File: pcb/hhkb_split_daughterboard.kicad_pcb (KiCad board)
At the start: 2 copper layers, 21 x 32 mm, 11 parts

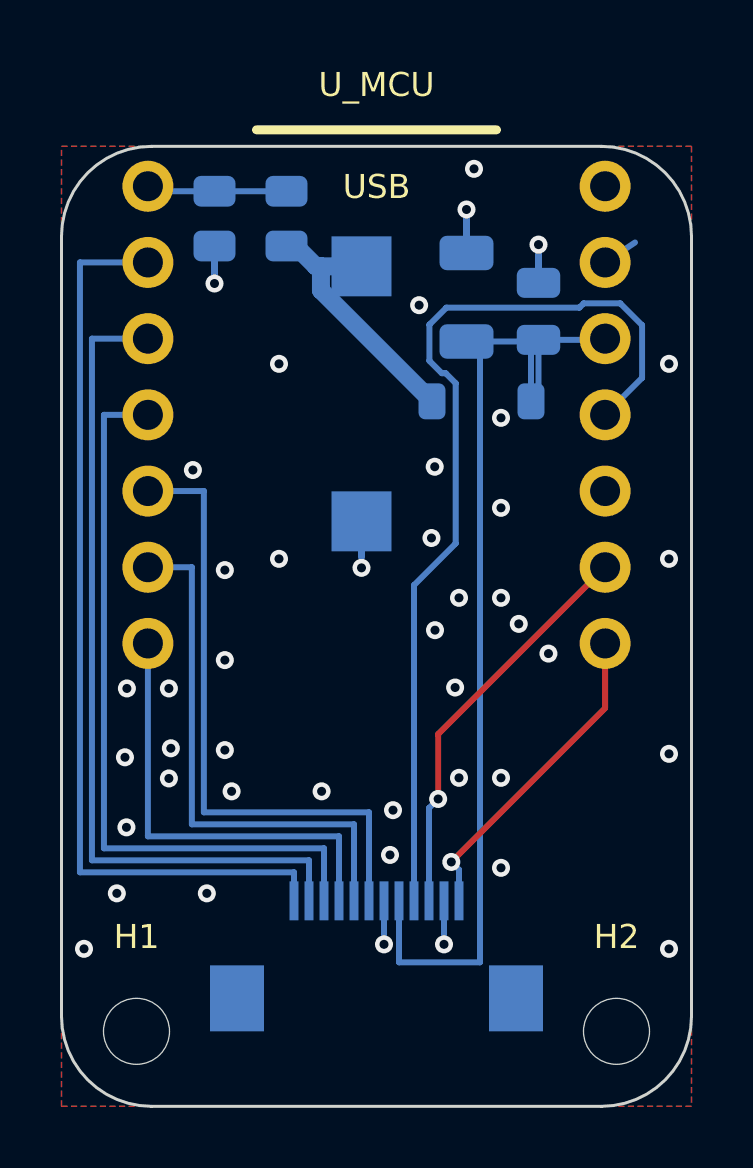
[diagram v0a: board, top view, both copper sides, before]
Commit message: 子基板の手配線の直角を、最小の 45 度 2 回に割った
利用者の指示「可能な限り最小のコーナーで 135 度 *2 に」。直角のまま
曲げると外側の角で銅が尖り、エッチングで過剰腐食を受けやすい。

点列を引く 3 か所（外側レーン・内側レーン・V3V3）が同じ形をしていたので、
面取り付きの `_polyline` に集約した。今後経路を変えても面取りは残る。

一辺は線幅と同じ 0.2mm。**見た目はほぼ角のまま**で、外側の角だけが
消えて 135 度が 2 つになる。それ以上大きくしても角の鋭さは変わらない。
線分が短くて両側に取れない折れは、その半分までに切り詰める。

実測: 45 度の区間が 20 本（配線後の基板でも 34 本残っている）。
子基板 DRC は 未配線 0 / 違反 1 で、面取りによる新しい違反は無い
（残る 1 件は V3V3 と GND ビアの 0.100mm。利用者の指示で保留中）。

Co-Authored-By: Claude Opus 5 (1M context) <noreply@anthropic.com>
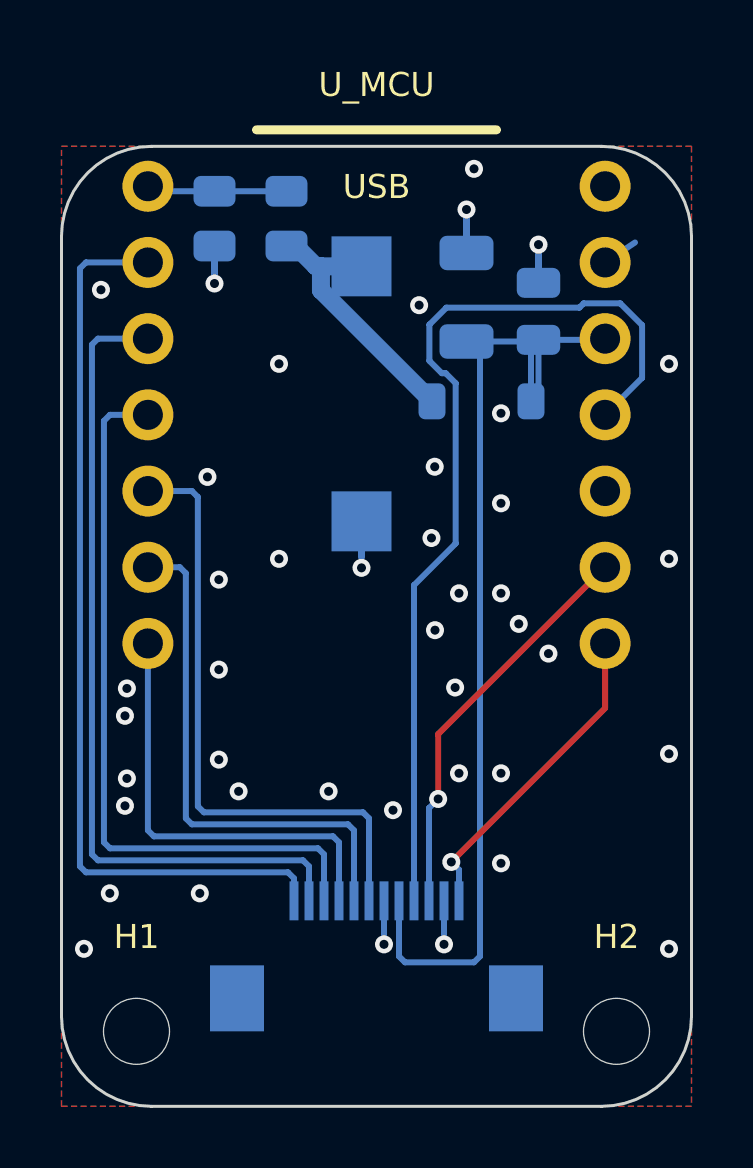
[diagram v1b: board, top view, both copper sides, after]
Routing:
- net GND: vias 44 -> 42

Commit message: 子基板の右列を、左列の鏡像として自分で引いた
利用者の指示「D1〜D6 を完璧に真似る形で、左右対称に」。右列は
Freerouting 任せだったので、左列と同じ規則で引くようにした。

XIAO は x=150.0 を挟んで左右対称なので、**鏡像は同じ y のパッドどうし**
（D1↔GND / D2↔3V3 / D3↔D10 / D4↔D9 / D5↔D8 / D6↔D7）。FFC は
n ↔ 13-n で写る。`_prewire_rows` に `side`（-1 左 / +1 右）を入れ、
左向きの直書き（min・-DB_W/2）を符号 1 つに畳んだ。

指摘を 3 つ受けて直した:
  - D7 が垂直に伸びていない … D6 の鏡像は D7。GND を外したことと
    垂直の有無は無関係だった
  - D4 の鏡像は D9 … 内側の順序を左列の鏡像 (D7,D8,D9) に揃えた
  - V3V3 が 2 経路で FFC に繋がる … `_prewire_power` の旧経路を削除。
    3V3 パッド ↔ FFC 2 番はレーンが引くので二重だった

**GND はレーンに載せず地板で受ける**（利用者の判断）。そのぶん外側は
2 本になるが、**位置は 3 本ぶんの幅に散らして真ん中を空ける**——
利用者の指示「D10 と離す意図で、鏡像の 3 本ラインの左端と右端と同様に」。
電源とデータ線の並走結合を、空いている枠を使って 0 コストで下げる。

⚠️ **この組み替えでケーブルの GND が 2 本から 1 本になった。**
SCK から最寄りの GND までが 0.5mm → 2.0mm に伸びている。効くのは
遷移が速い SCK 1 本で、どれだけ悪化するかは実測していない。
逃げ道は決めてある（D9=SPARE2 を両基板で GND へジャンパ）。

検査は「GND が 2 本」を数えるのをやめ、**距離そのもの**を見るように
書き換えた（`test_how_far_the_return_path_is`）。本数は手段で、目的は
戻り経路の短さ。故意に壊して距離 7 で落ちることを確認した。
`test_the_rules_actually_bite` の変異 1 件が**元と同じ値を代入する
空振り**になっていたのも、その検査自身が捕まえたので直した。

子基板 DRC: 違反 0 / 未配線 0。保留していた V3V3-GND の 0.100mm も
旧経路の削除で消えた。主基板の SPARE/SPARE2 が片側 1 ピンなので
test_circuit が 2 件赤。左右の基板はこれから直す。

Co-Authored-By: Claude Opus 5 (1M context) <noreply@anthropic.com>
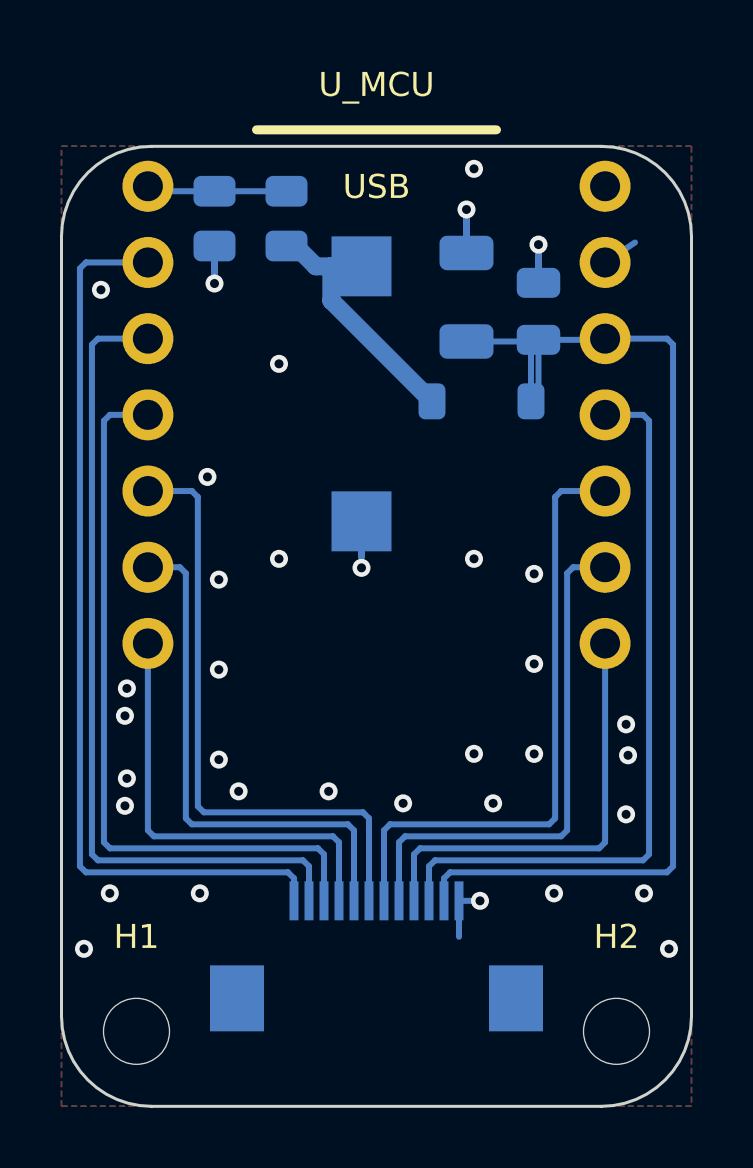
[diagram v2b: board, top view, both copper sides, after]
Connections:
- J_MAIN pad 1: CS -> GND
- J_MAIN pad 2: GND -> V3V3
- J_MAIN pad 3: SPI_SCK -> SPI_MOSI
- J_MAIN pad 4: SPI_MOSI -> CS
- J_MAIN pad 5: V3V3 -> SPI_SCK
- J_MAIN pad 6: GND -> SPARE2
- U_MCU pad D9: (no net) -> SPARE2
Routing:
- net SPARE2: track 0.00 -> 20.7 mm
- net SPI_MOSI: track 31.4 -> 24.6 mm
- net SPI_SCK: track 13.6 -> 17.6 mm, vias 1 -> 0
- net CS: track 10.8 -> 14.7 mm, vias 1 -> 0
- net GND: track 16.8 -> 13.4 mm, vias 42 -> 35
- net V3V3: track 34.2 -> 37.0 mm

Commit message: 行のネット名を「ケーブル上の位置」にし、行の並びを左右で別々に決めた
利用者の指摘「左右で ROW の順番を変えてもいい（左右で違う FW になるのは
確定している）。そういう意味で、DB の ROWx というピン名前付は不適切に
なるかもしれません」。理由は「左右 MAIN PCB を可能な限り鏡像にしている
がゆえに、どの FFC ピンがどの行に最適かが変わってくる」。

**ネット名を ROW0..4 → ROW_A..E に改めた。**名前が指すのは行番号ではなく
**ケーブル上の位置**（子基板のレーン）。行番号を名前にすると、左右で違う
行を同じ線に載せた瞬間に嘘になる（左の ROW2 が右では行 4 を運ぶ）。

**`row-gpios` を共通の dtsi から左右の overlay へ移した。**行がどの GPIO に
来るかは左右で物理的に違う——J_DB が左は板の右端・右は左端にあり、同じ
FFC のピンでも行バスへ近づく向きが逆。共通に 1 つだけ書くと、どちらかの
基板で必ず交差が出る。`matrix.row_nets(half)` が唯一の出所になった。

**割り当ての考え方も利用者の指摘で組み直した。**当初は「上へ行く群／下へ
行く群」で交差を数えていたが、正しくは **J_DB から遠い行ほど、パッド列で
「板の内側」の枠へ**。遠くまで行く枝を内側に置くと他の枝を跨がずに列を
離れられる。左右で並びが逆になる（12 番の板端／内側の意味が入れ替わる）。

    左: 行4=ROW_E 行3=ROW_D 行0=ROW_C 行2=ROW_B 行1=ROW_A
    右: 行4=ROW_A 行3=ROW_B 行0=ROW_C 行2=ROW_D 行1=ROW_E

**3 基板とも DRC 違反 0 / 未配線 0。**逆向きだと左 1 本・右 3 本が未配線に
なることを実測した（総当たりのモデルだけでは決まらなかった）。

検査は新しい構造に合わせて書き換え、**故意に壊して落ちることを確認した**
（overlay のピンを 1 つ変える／行を 2 つ入れ替える）。「左右で並びが違って
よい」ことも検査に書いて、揃える方向の変更が入らないようにした。

⚠️ 主基板の SPARE/SPARE2 が片側 1 ピンなので test_circuit が 2 件赤。
これは左右基板の残作業（J_DB の予備ピンの行き先）で解消する。

Co-Authored-By: Claude Opus 5 (1M context) <noreply@anthropic.com>
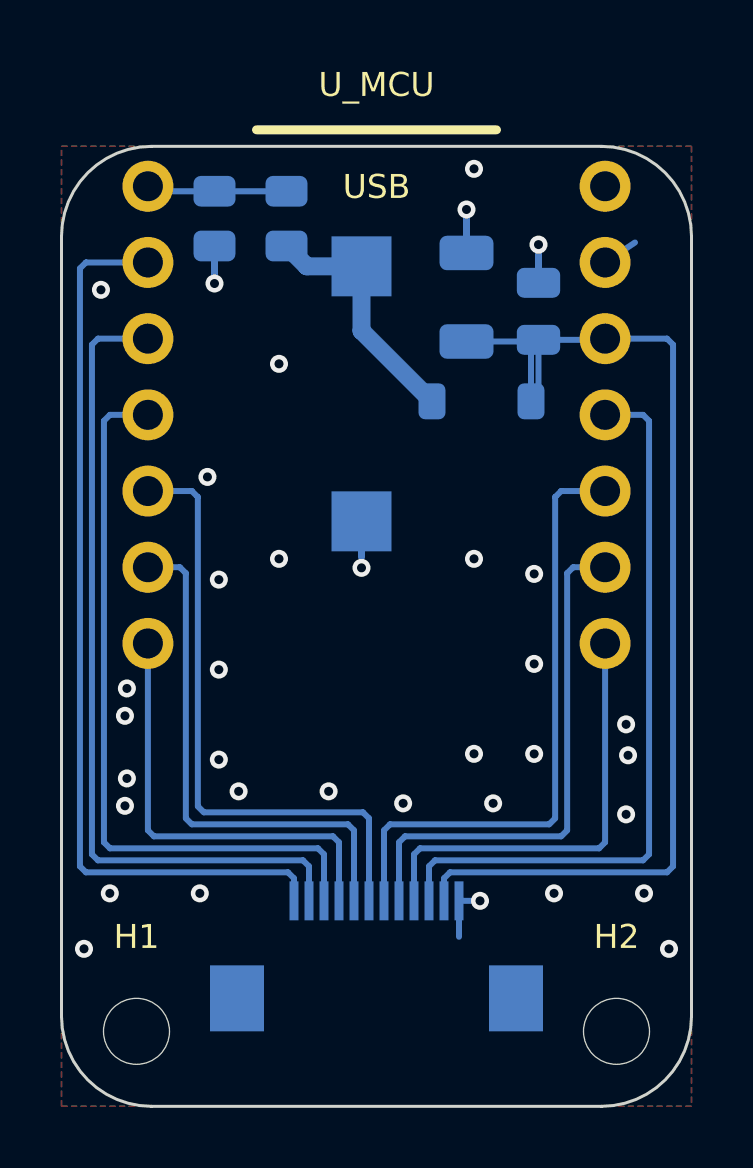
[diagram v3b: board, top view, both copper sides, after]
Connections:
- net ROW0 renamed ROW_E
- net ROW1 renamed ROW_C
- net ROW2 renamed ROW_D
- net ROW3 renamed ROW_A
- net ROW4 renamed ROW_B

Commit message: 子基板の未配線 4 件を消し、GND スタブの重複とシルクを直した
**未配線 4 件（VBATT_SW / VBATT_SENSE）の正体は Freerouting への入力だった。**
DSN に `(autoroute_settings)` があるだけで、Freerouting 2.3.0 が子基板の
ネットを 1 本も見なくなる。同じ DSN でブロックの有無だけを変えた実測:

    あり … "started with 0 unrouted nets" / SES 18 行（空）
    なし … "started with 4 unrouted nets" / SES 98 行

中身は関係ない（fanout / start_ripup_costs / layer_rule を 4 通り試して
すべて 0）。4 接続は直線経路に障害物が無く（2.2〜4.0mm・邪魔なし）、
「密集して引けない」のではなく**渡っていなかった**。子基板だけ外す。
主基板は正常に働く（左 started_with=60）ので残す。

**GND の引き出しが 1 パッドに 2 本生えていた**（利用者「GND は同じベタに
2 つ生えています。両方いるか、という事です」）。`_prewire_power` と
`gnd_fanout.place` がどちらも同じパッドから B.Cu へ出るため、6 パッドに
11 本。うち 4 組は始点も向きも同じで、1.2mm 側はビアへ向かうスタブの
完全な部分区間だった。ビアで受けるパッドには引かない。

さらに **U_MCU の GND は PTH**（穴 1.0mm）で、穴自体が両面のベタを貫く
ので引き出しは元から不要だった。「最寄りビアまで 3.22mm」と書いたのは
スタブの端から測った誤りで、中心からは 2.13mm。そもそも距離の問題では
なかった。引き出しは 11 本 → 0 本になり、未配線は増えていない。

**肩の高さを左右で揃えた**（利用者「この微妙に高さ違うのを直してほしい」）。
`over` を `i`（この列の何本目か）ではなく `slot`（枠の番号）で数える。
本数の違う列で同じ役割の線が違う高さになっていた。交差は増えない
（全 11 ネットを総当たりで交差判定して 0 件）。V3V3 だけは鏡像にならないが
利用者の判断で現状維持。

**V3V3 の往復を消した**（利用者「C_DB と D_PWR の間で不要に 2 本」）。
x 順の鎖に、一列から 2mm 下がった D_PWR が挟まって往復していた。
横一列のものだけで鎖を作り、外れたものは最寄りへ 1 本。

**ビアの空白を埋めた**（利用者「D6, D7 の下の領域、GND とビア打てないの？」）。
格子は λ/10 = 6.5mm と粗く、21x32mm では格子点が十数個しかないので
1 点が塞がると周りが丸ごと空く。実測で打てる点が 168 箇所あったのに
0 個だった。ピッチは動かさず、外れた点だけ半ピッチ以内で探し直す。
格子 7 → 14 個。

**シルクは利用者が KiCad で並べたものを出所にする**（`POWER_PLACE` と同じ）。
4 方向を試して空きを探す実装を書いたが、判定を厳しくするほど
「どこも当たる＝動かさない」が増え、13 → 10 → 13 → 15 件と悪化した。
機械的な 4 方向では解が無い。`SILK_REF` に固定し、並べ直したときは
`_read_silk_from` で吸い出す（手で書き写さない）。

R_HI / SW_PWR の配置も利用者の基板から読み直した（11 部品すべて一致）。

子基板: 違反 0 / 未配線 0 / 警告 13 → 5。基板の検査 90 件通過。

Co-Authored-By: Claude Opus 5 (1M context) <noreply@anthropic.com>
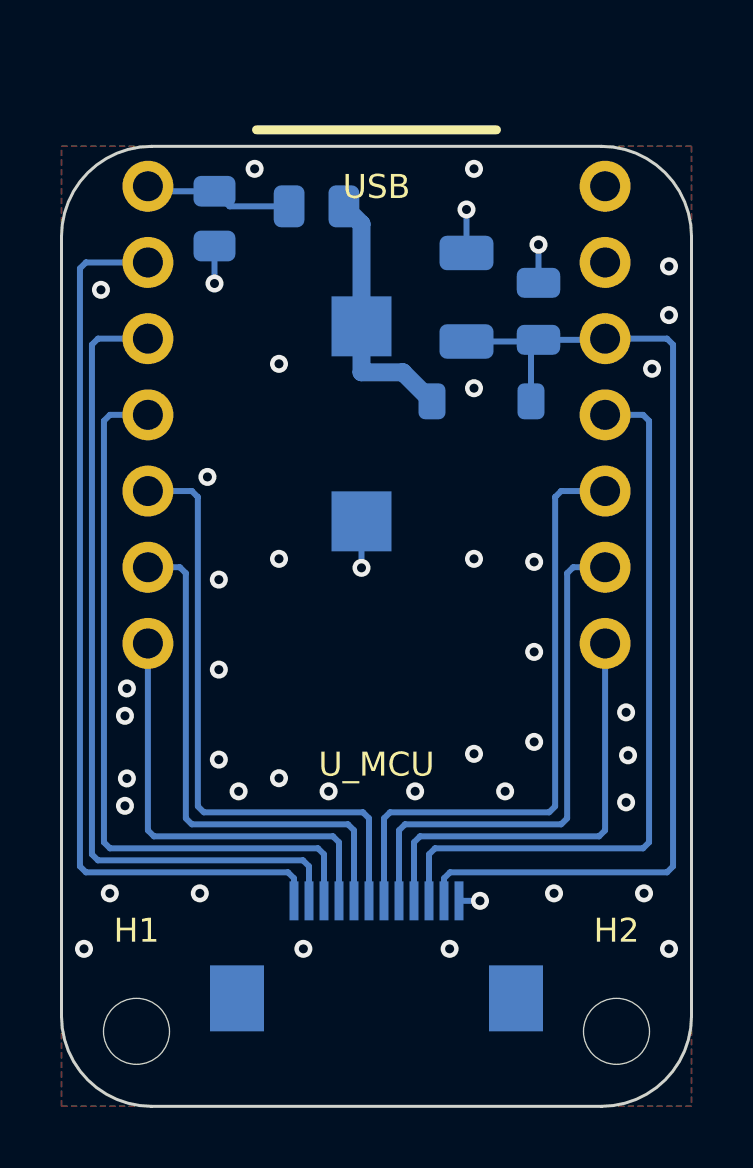
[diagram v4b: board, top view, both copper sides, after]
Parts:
- moved SW_PWR_1 2.00 mm to (149.5, 90.0)
- moved R_HI 1.08 mm to (148.0, 86.0), turned to 180 degrees
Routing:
- net GND: track 13.4 -> 6.23 mm, vias 35 -> 43
- net V3V3: track 37.0 -> 35.3 mm

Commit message: 子基板のアンテナ禁止域を 3.5 角から 7.5 角へ広げ、配線とビアも禁止した
アンテナの実体の四方に 2.0mm の逃げを取る。ベタだけでなく配線とビアも
禁止する（両面）。3 基板とも DRC 違反 0・未配線 0。

**2.0mm の出所**: 4 方向を同時に広げて信号配線・パッドに当たらない上限が
2.2mm（pcb/unrouted/ の板で実測）。そこから 0.2mm 引いた。
Seeed が XIAO 上で確保している 1.76mm を上回る——ただし**これは公開仕様
ではない**。wiki・SOM データシート・LCSC を全文検索したが keepout の mm
指定は 1 つも無く、公式 KiCad プロジェクト（V1.1）から実測した値。

**配線とビアを禁止できた理由**: 「FFC から XIAO への 12 本が必ず横切るので
禁止すると 14 件の違反」というコメントは、帯が板の全幅だった頃の記録で、
x 4.5mm に絞った #41 以降は当てはまらない。実測で帯に掛かるものは 0 件。

**gnd_fanout の根本原因も直した**: ビアを置く経路が 2 つある（spots と
stitch）のに、`_obstacles` 側だけがルール領域を見ていた。`spots` は
`_pad_boxes` しか見ないので、パッド直近のファンアウトのビアだけが禁止域に
入り、DRC が items_not_allowed を 1 件出した。両方に入れ、かつ**ビアの
外径ぶん膨らませる**（判定側が見るのはビアの中心なので、箱のままだと
中心が外なら通って銅が中に入る）。

検査は y 方向の拡大が無検査だった穴を塞いだ（逃げを 0 にしても 13 件
全部が通っていた）。故意に壊して落ちることを確認済み。禁止内容
（tracks/vias/copperpour が not_allowed か）も見るようにした。

⚠️ **未解決**: 禁止域が XIAO の中心から左に 1.9mm ずれて見える。
`ANTENNA_X = -1.9` の符号を実機で裏取りできていない（interface.py 自身が
「裏返すと左右が入れ替わり結論が逆になる」と警告している値）。

pytest tools は未実行（test_daughterboard.py の 13 件のみ通過を確認）。

Co-Authored-By: Claude Opus 5 (1M context) <noreply@anthropic.com>
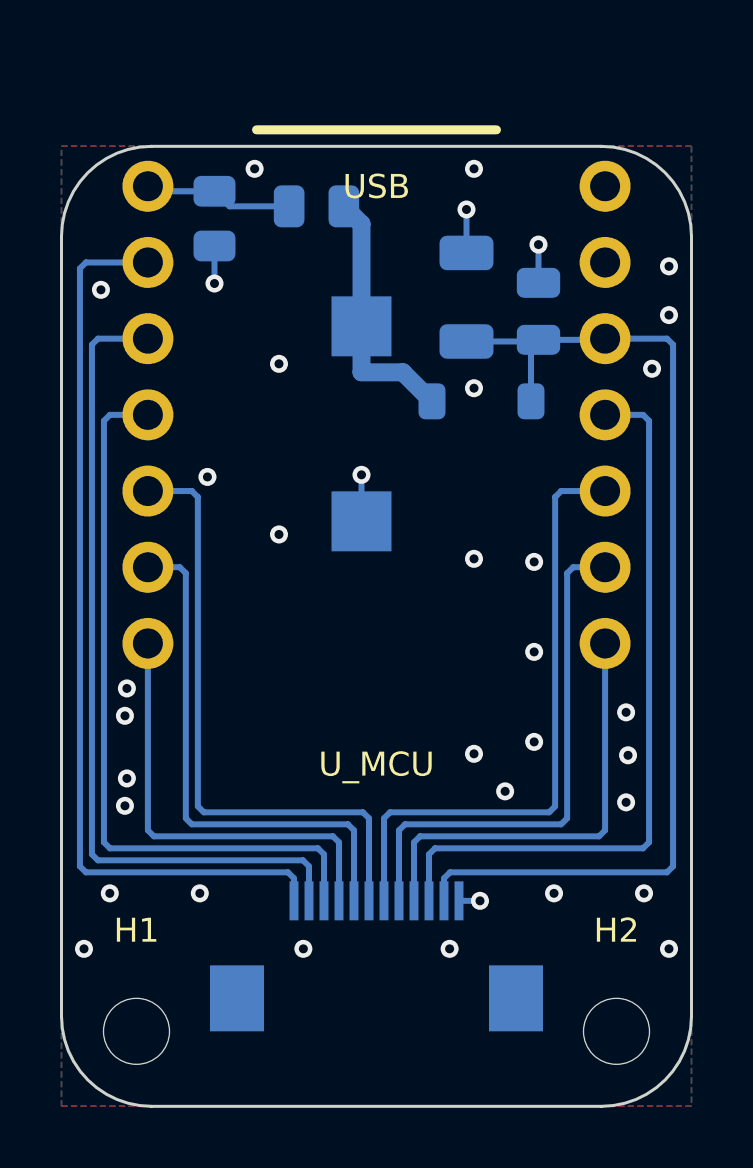
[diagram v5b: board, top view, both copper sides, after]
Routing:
- net GND: vias 43 -> 36

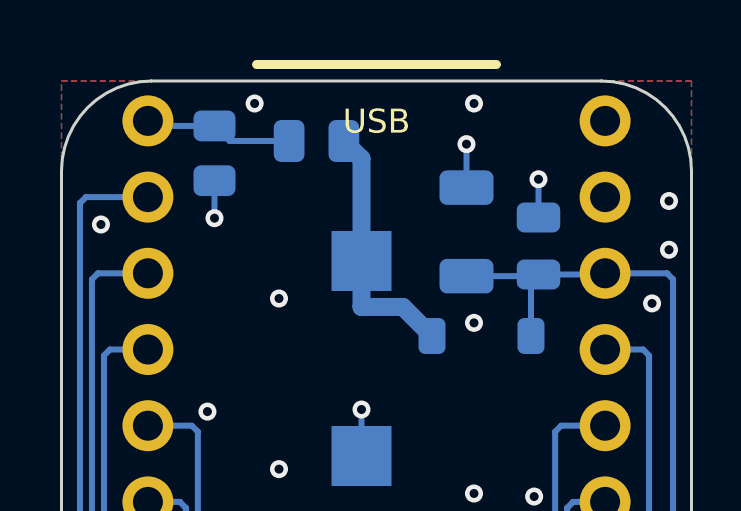
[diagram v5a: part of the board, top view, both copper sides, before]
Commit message: FFC コネクタの X を子基板と揃えた（左 3.52 → 0.40mm・右 1.35 → 0.00mm）
本体基板の J_DB と子基板の J_MAIN は**どちらも口が手前を向いている**のに
X がずれていて、ずれたぶん FFC が横へ折れていた（利用者の指摘）。

**座標を手で書かず、子基板の中心から取る。**直書きだとキー配列や
ケースの幅が動いた日に黙ってずれる。そのため
inner_sign / battery_x_center / daughterboard_x_center を gen_case.py
（build123d 依存で KiCad の Python から読めない）から interface.py へ移し、
gen_case は再輸出だけにした。二重に持っていた DB_W も出所を 1 つにし、
WALL / BATT_X は突き合わせの assert を置いた。

揃えた先に部品が居ることがあるので、_snap_clear_of_courtyards が
当たらない最寄りへ逃がし、ずれ量を印字する（左は D12 が 0.36mm 掛かるので
+0.40mm、右は 0.00mm で完全一致）。**スイッチは障害物に数えない**——
実装面が違う（スイッチは表・コネクタは裏の SMD）ので重なってよく、
数えると右が 3.95mm 逃げて揃える前より悪くなる。

## 一緒に見つかった別のバグ

GUIDE_VIAS の V3V3 中継ビアが (72.75, 84.0) と直書きされていた。
J_DB が動いた瞬間、**V3V3 のパッド(76.10)から外れて ROW_B のパッド(72.60)
の上に乗り**、ROW_B が未配線になる。パッドから座標を取るようにした。
これは移設前から潜在していたもので、実際にベースラインの右基板は
未配線 2 件（ROW_B と GND 離島）だった。

## 検証

- 再生成 → 自動配線 → DRC: 左 0/0・右 違反 0/未配線 1・子基板 0/0
  右の 1 件は U1 の GND 離島で、**ベースラインにもあった**（2 → 1 に減った）。
  コネクタ位置と無関係な既存の不具合なので範囲を広げず残す
- ずれ量は pcb_parts.json を取り直したうえで**実 STEP 形状から実測**
- gen_assembly の実形状の干渉 0 / refresh_view.sh で .blend も出し直し
- pytest tools: 437 passed / 3 failed。**3 件とも着手前から赤**
  （SPARE ネット 2 件は stash して確認済み、右の未配線 1 件は上記）

Co-Authored-By: Claude Opus 5 (1M context) <noreply@anthropic.com>
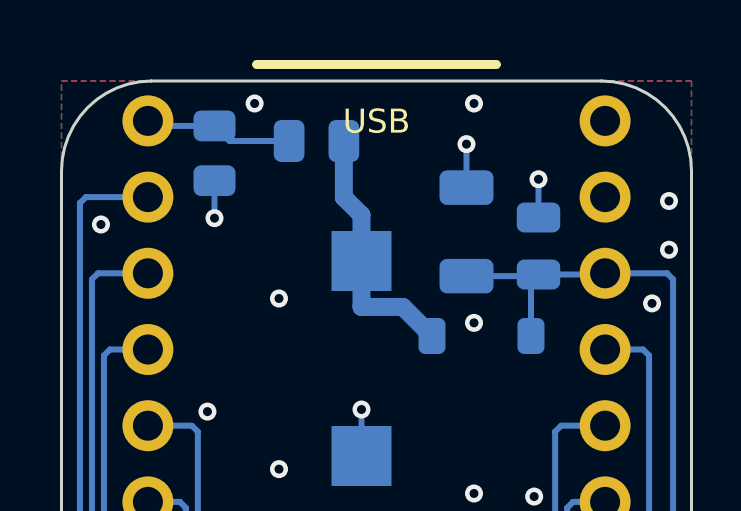
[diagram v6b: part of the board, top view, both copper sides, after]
